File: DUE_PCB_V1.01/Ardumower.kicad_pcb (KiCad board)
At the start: 2 copper layers, 169.3 x 95.5 mm, 86 parts, among them J1 I2C_1, J10 Bumper Left, J11 Bumper Right, J12 P_Left, J13 P_Right, J14 Sonar_R, J15 Sonar_C, J16 Sonar_L, J17 US1, J18 US2, J19 US3, J2 I2C_2, J20 Button, J21 5V IN, J22 Remote, J23 PCB_2, J24 3.3V IN, J25 TX0/RX0, J26 TX1/RX1, J27 TX2/RX2, J28 GPS_TX/GPS_RX, J29 Motor_Right1, J3 I2C_3, J30 Motor_Right2, J31 Motor_Left1, J32 Motor_Left2, J33 Cutter_Motor, J34 ODORight1, J35 ODORight2, J36 ODOLeft1, J37 ODOLeft2, J38 ODOCutter, J4 DS3231 RTC, J5 9V IN, J6 Drop_Left, J7 Drop_Right, J8 Tilt, J9 Rain

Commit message: Start ro add Bernard changes from 1.02
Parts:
- added B1: SPARKFUN_LOGIC_LEVEL_CONVERTER, Boards:SPARKFUN_LOGIC_LEVEL_CONVERTER, F.Cu at (109.3, 83.9)

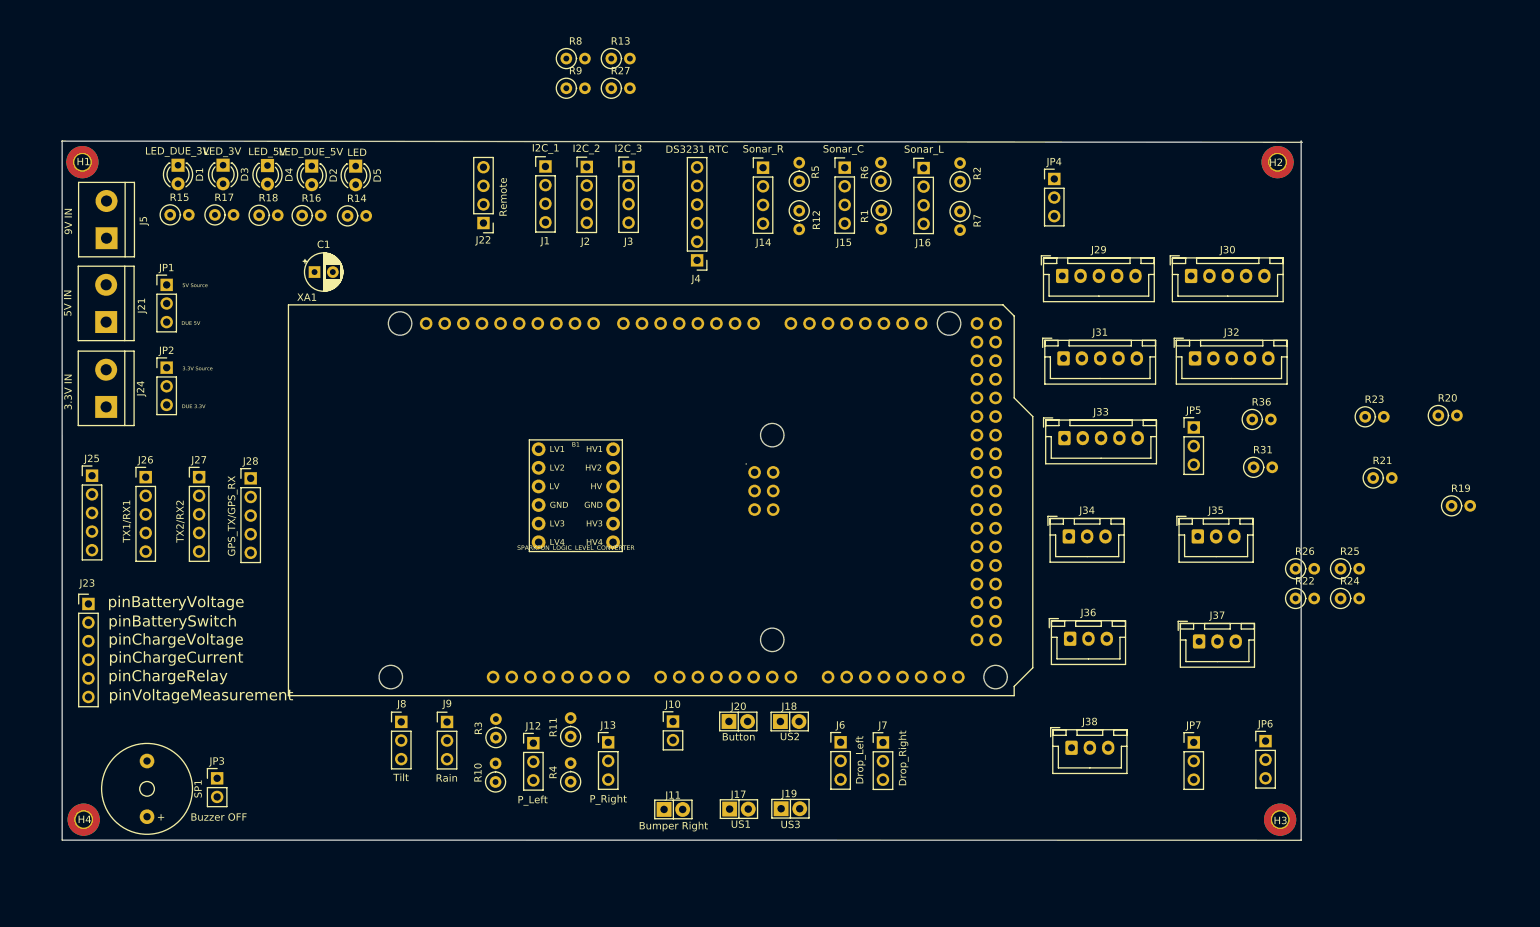
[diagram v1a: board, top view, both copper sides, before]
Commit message: Add Reserve Pin Connectors
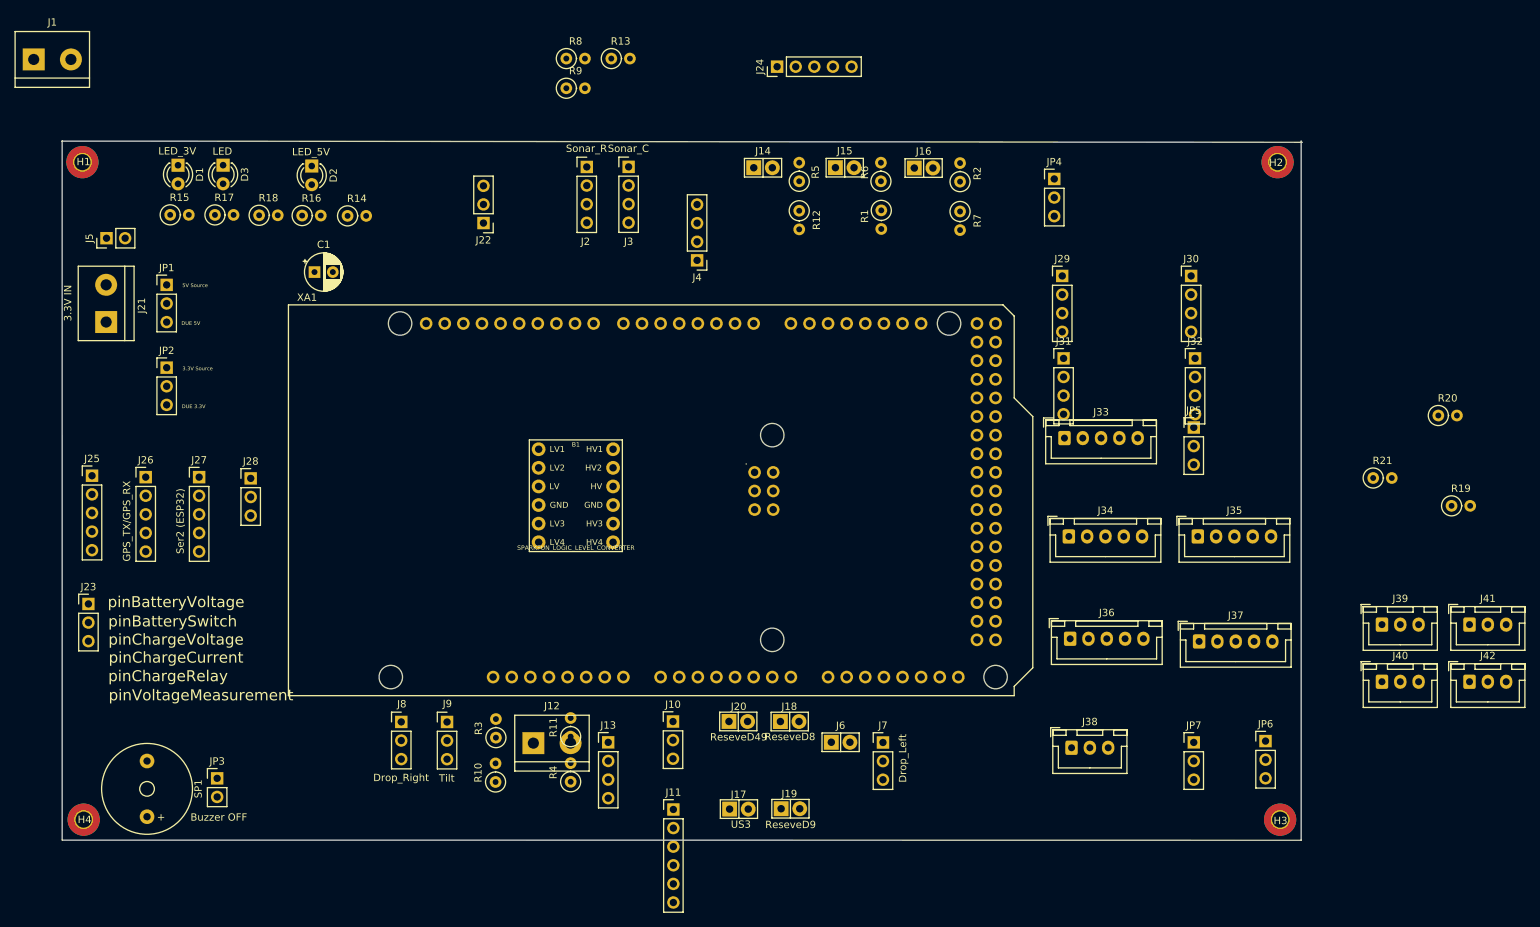
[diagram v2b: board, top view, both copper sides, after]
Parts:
- removed D4: LED_5V, LED_THT:LED_D3.0mm
- removed D5: LED, LED_THT:LED_D3.0mm
- removed R22, R31: 1KO, Resistor_THT:R_Axial_DIN0207_L6.3mm_D2.5mm_P2.54mm_Vertical
- removed R23, R24, R25, R26, R36: 1.5KO, Resistor_THT:R_Axial_DIN0207_L6.3mm_D2.5mm_P2.54mm_Vertical
- removed R27: XXX, Resistor_THT:R_Axial_DIN0207_L6.3mm_D2.5mm_P2.54mm_Vertical
- added J39: ODORight2, Connector_JST:JST_XH_B3B-XH-A_1x03_P2.50mm_Vertical, F.Cu at (219.4, 101.5)
- added J40: ODOLeft1, Connector_JST:JST_XH_B3B-XH-A_1x03_P2.50mm_Vertical, F.Cu at (219.4, 109.3)
- added J41: ODOLeft2, Connector_JST:JST_XH_B3B-XH-A_1x03_P2.50mm_Vertical, F.Cu at (231.3, 101.5)
- added J42: ODOCutter, Connector_JST:JST_XH_B3B-XH-A_1x03_P2.50mm_Vertical, F.Cu at (231.3, 109.3)
- D1: value LED_DUE_3V -> LED_3V
- D2: value LED_DUE_5V -> LED_5V
- D3: value LED_3V -> LED
- J1: value I2C_1 -> 9V IN; footprint Connector_PinHeader_2.54mm:PinHeader_1x04_P2.54mm_Vertical -> TerminalBlock:TerminalBlock_bornier-2_P5.08mm
- J10: value Bumper Left -> Rain; footprint Connector_PinHeader_2.54mm:PinHeader_1x02_P2.54mm_Vertical -> Connector_PinHeader_2.54mm:PinHeader_1x03_P2.54mm_Vertical
- J11: value Bumper Right -> PCB_2; footprint Zimprich:Pin_Header_KK110_1x02_3D -> Connector_PinHeader_2.54mm:PinHeader_1x06_P2.54mm_Vertical
- J12: value P_Left -> 5V IN; footprint Connector_PinHeader_2.54mm:PinHeader_1x03_P2.54mm_Vertical -> TerminalBlock:TerminalBlock_bornier-2_P5.08mm
- J13: value P_Right -> Remote; footprint Connector_PinHeader_2.54mm:PinHeader_1x03_P2.54mm_Vertical -> Connector_PinHeader_2.54mm:PinHeader_1x04_P2.54mm_Vertical
- J14: value Sonar_R -> Button; footprint Connector_PinHeader_2.54mm:PinHeader_1x04_P2.54mm_Vertical -> Zimprich:Pin_Header_KK110_1x02_3D
- J15: value Sonar_C -> US1; footprint Connector_PinHeader_2.54mm:PinHeader_1x04_P2.54mm_Vertical -> Zimprich:Pin_Header_KK110_1x02_3D
- J16: value Sonar_L -> US2; footprint Connector_PinHeader_2.54mm:PinHeader_1x04_P2.54mm_Vertical -> Zimprich:Pin_Header_KK110_1x02_3D
- J17: value US1 -> US3
- J18: value US2 -> ReseveD8
- J19: value US3 -> ReseveD9
- J2: value I2C_2 -> Sonar_R
- J20: value Button -> ReseveD49
- J21: value 5V IN -> 3.3V IN
- J22: value Remote -> P_Left; footprint Connector_PinHeader_2.54mm:PinHeader_1x04_P2.54mm_Vertical -> Connector_PinHeader_2.54mm:PinHeader_1x03_P2.54mm_Vertical
- J23: value PCB_2 -> P_Right; footprint Connector_PinHeader_2.54mm:PinHeader_1x06_P2.54mm_Vertical -> Connector_PinHeader_2.54mm:PinHeader_1x03_P2.54mm_Vertical
- J24: value 3.3V IN -> Ser0; footprint TerminalBlock:TerminalBlock_bornier-2_P5.08mm -> Connector_PinHeader_2.54mm:PinHeader_1x05_P2.54mm_Vertical
- J25: value TX0/RX0 -> Ser1
- J26: value TX1/RX1 -> GPS_TX/GPS_RX
- J27: value TX2/RX2 -> Ser2 (ESP32)
- J28: value GPS_TX/GPS_RX -> Buzzer; footprint Connector_PinHeader_2.54mm:PinHeader_1x05_P2.54mm_Vertical -> Connector_PinHeader_2.54mm:PinHeader_1x03_P2.54mm_Vertical
- J29: value Motor_Right1 -> I2C0_1; footprint Connector_JST:JST_XH_B5B-XH-A_1x05_P2.50mm_Vertical -> Connector_PinHeader_2.54mm:PinHeader_1x04_P2.54mm_Vertical
- J3: value I2C_3 -> Sonar_C
- J30: value Motor_Right2 -> I2C0_2; footprint Connector_JST:JST_XH_B5B-XH-A_1x05_P2.50mm_Vertical -> Connector_PinHeader_2.54mm:PinHeader_1x04_P2.54mm_Vertical
- J31: value Motor_Left1 -> I2C1_1; footprint Connector_JST:JST_XH_B5B-XH-A_1x05_P2.50mm_Vertical -> Connector_PinHeader_2.54mm:PinHeader_1x04_P2.54mm_Vertical
- J32: value Motor_Left2 -> I2C1_2; footprint Connector_JST:JST_XH_B5B-XH-A_1x05_P2.50mm_Vertical -> Connector_PinHeader_2.54mm:PinHeader_1x04_P2.54mm_Vertical
- J33: value Cutter_Motor -> Motor_Right1
- J34: value ODORight1 -> Motor_Right2; footprint Connector_JST:JST_XH_B3B-XH-A_1x03_P2.50mm_Vertical -> Connector_JST:JST_XH_B5B-XH-A_1x05_P2.50mm_Vertical
- J35: value ODORight2 -> Motor_Left1; footprint Connector_JST:JST_XH_B3B-XH-A_1x03_P2.50mm_Vertical -> Connector_JST:JST_XH_B5B-XH-A_1x05_P2.50mm_Vertical
- J36: value ODOLeft1 -> Motor_Left2; footprint Connector_JST:JST_XH_B3B-XH-A_1x03_P2.50mm_Vertical -> Connector_JST:JST_XH_B5B-XH-A_1x05_P2.50mm_Vertical
- J37: value ODOLeft2 -> Cutter_Motor; footprint Connector_JST:JST_XH_B3B-XH-A_1x03_P2.50mm_Vertical -> Connector_JST:JST_XH_B5B-XH-A_1x05_P2.50mm_Vertical
- J38: value ODOCutter -> ODORight1
- J4: value DS3231 RTC -> Sonar_L; footprint Connector_PinHeader_2.54mm:PinHeader_1x06_P2.54mm_Vertical -> Connector_PinHeader_2.54mm:PinHeader_1x04_P2.54mm_Vertical
- J5: value 9V IN -> Bumper Left; footprint TerminalBlock:TerminalBlock_bornier-2_P5.08mm -> Connector_PinHeader_2.54mm:PinHeader_1x02_P2.54mm_Vertical
- J6: value Drop_Left -> Bumper Right; footprint Connector_PinHeader_2.54mm:PinHeader_1x03_P2.54mm_Vertical -> Zimprich:Pin_Header_KK110_1x02_3D
- J7: value Drop_Right -> Drop_Left
- J8: value Tilt -> Drop_Right
- J9: value Rain -> Tilt
- R10, R11: value 1.5KO -> XXX
- R12: value 2KO -> 1KO
- R13: value XXX -> 1KO
- R14, R15: value 100 -> 1KO
- R16: value 220 -> 1KO
- R17: value 100 -> 1.5KO
- R18: value 220 -> 1.5KO
- R19, R20, R21, R3, R4: value 1KO -> 1.5KO
- R5: value 1KO -> XXX
- R6: value 2KO -> XXX
- R7: value 2KO -> 100
- R8: value XXX -> 100
- R9: value XXX -> 220
- moved J24 102.7 mm to (136.8, 25.4)
- moved J1 71.4 mm to (35.3, 24.4)
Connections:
- J1 pad 1: +3V3 -> GND
- J1 pad 2: GND -> +9V
- J10 pad 1: GND -> +3V3
- J10 pad 2: pinBumperLeft -> GND
- J11 pad 1: GND -> pinBatteryVoltage
- J11 pad 2: pinBumperRight -> pinBatterySwitch
- J12 pad 1: +5V -> GND
- J12 pad 2: GND -> Net-(J12-Pad2)
- J13 pad 1: +5V -> pinRemoteSpeed
- J13 pad 2: GND -> pinRemoteSteer
- J13 pad 3: Net-(J13-Pad3) -> pinRemoteMow
- J14 pad 1: +5V -> GND
- J14 pad 2: GND -> pinButton
- J15 pad 1: +5V -> GND
- J15 pad 2: GND -> pinUserSwitch1
- J16 pad 1: +5V -> GND
- J16 pad 2: GND -> pinUserSwitch2
- J17 pad 2: pinUserSwitch1 -> pinUserSwitch3
- J18 pad 2: pinUserSwitch2 -> ReservePinD8
- J19 pad 2: pinUserSwitch3 -> ReservePinD9
- J2 pad 3: SDA0 -> pinSonarRightEcho
- J2 pad 4: SCL0 -> pinSonarRightTrigger
- J20 pad 2: pinButton -> ReservePinD49
- J22 pad 1: pinRemoteSpeed -> +5V
- J22 pad 2: pinRemoteSteer -> GND
- J22 pad 3: pinRemoteMow -> Net-(J22-Pad3)
- J23 pad 1: pinBatteryVoltage -> +5V
- J23 pad 2: pinBatterySwitch -> GND
- J23 pad 3: pinChargeVoltage -> Net-(J23-Pad3)
- J24 pad 1: GND -> +3V3
- J24 pad 2: Net-(J24-Pad2) -> GND
- J25 pad 3: RX0 -> RX1
- J25 pad 4: TX0 -> TX1
- J26 pad 3: RX1 -> (no net)
- J26 pad 4: TX1 -> TX3
- J28 pad 3: GPS_RX -> pinBuzzer
- J29 pad 1: pinMotorRightPWM -> +3V3
- J29 pad 2: pinMotorRightDir -> GND
- J29 pad 3: pinMotorEnable -> SDA0
- J29 pad 4: Net-(J29-Pad4) -> SCL0
- J3 pad 3: SDA1 -> pinSonarCenterEcho
- J3 pad 4: SCL1 -> pinSonarCenterTrigger
- J30 pad 1: pinMotorRight2PWM -> +3V3
- J30 pad 2: pinMotorRightDir -> GND
- J30 pad 3: pinMotorEnable -> SDA0
- J30 pad 4: Net-(J29-Pad4) -> SCL0
- J31 pad 1: pinMotorLeftPWM -> +3V3
- J31 pad 2: pinMotorLeftDir -> GND
- J31 pad 3: pinMotorEnable -> SDA1
- J31 pad 4: Net-(J29-Pad4) -> SCL1
- J32 pad 1: pinMotorLeft2PWM -> +3V3
- J32 pad 2: pinMotorLeftDir -> GND
- J32 pad 3: pinMotorEnable -> SDA1
- J32 pad 4: Net-(J29-Pad4) -> SCL1
- J33 pad 1: pinMotorMowPWM -> pinMotorRightPWM
- J33 pad 2: pinMotorMowDir -> pinMotorRightDir
- J33 pad 3: pinMotorMowEnable -> pinMotorEnable
- J34 pad 1: Net-(J34-Pad1) -> pinMotorRight2PWM
- J34 pad 2: Net-(J34-Pad2) -> pinMotorRight2Dir
- J34 pad 3: GND -> pinMotorEnable
- J35 pad 1: Net-(J35-Pad1) -> pinMotorLeftPWM
- J35 pad 2: Net-(J34-Pad2) -> pinMotorLeftDir
- J35 pad 3: GND -> pinMotorEnable
- J36 pad 1: Net-(J36-Pad1) -> pinMotorLeft2PWM
- J36 pad 2: Net-(J34-Pad2) -> pinMotorLeft2Dir
- J36 pad 3: GND -> pinMotorEnable
- J37 pad 1: Net-(J37-Pad1) -> pinMotorMowPWM
- J37 pad 2: Net-(J34-Pad2) -> pinMotorMowDir
- J37 pad 3: GND -> pinMotorMowEnable
- J4 pad 1: (no net) -> +3V3
- J4 pad 2: (no net) -> GND
- J4 pad 3: SCL1 -> pinSonarLeftEcho
- J4 pad 4: SDA1 -> pinSonarLeftTrigger
- J5 pad 2: +9V -> pinBumperLeft
- J6 pad 1: +3V3 -> GND
- J6 pad 2: GND -> pinBumperRight
- J7 pad 3: pinDropRight -> pinDropLeft
- J8 pad 3: pinTilt -> pinDropRight
- J9 pad 3: pinRain -> pinTilt
- JP1 pad 1: Net-(J21-Pad2) -> Net-(J12-Pad2)
- JP2 pad 1: Net-(J24-Pad2) -> Net-(J21-Pad2)
- JP4 pad 2: Net-(J29-Pad4) -> Net-(J33-Pad4)
- JP5 pad 2: Net-(J33-Pad4) -> Net-(J37-Pad4)
- JP6 pad 2: Net-(J34-Pad2) -> Net-(J38-Pad2)
- JP7 pad 2: Net-(J38-Pad2) -> Net-(J42-Pad2)
- R1 pad 1: Net-(J15-Pad3) -> Net-(J22-Pad3)
- R1 pad 2: pinSonarCenterEcho -> pinPerimeterLeft
- R10 pad 1: Net-(J12-Pad3) -> SDA0
- R10 pad 2: GND -> +3V3
- R11 pad 1: Net-(J13-Pad3) -> SDA1
- R11 pad 2: GND -> +3V3
- R12 pad 1: Net-(J14-Pad3) -> pinOdometryRight
- R12 pad 2: GND -> Net-(J38-Pad1)
- R13 pad 1: SDA0 -> pinOdometryRight2
- R13 pad 2: +3V3 -> Net-(J39-Pad1)
- R14 pad 1: pinLED -> pinOdometryLeft
- R14 pad 2: Net-(D5-Pad2) -> Net-(J40-Pad1)
- R15 pad 1: Net-(D1-Pad2) -> pinOdometryLeft2
- R15 pad 2: DUE_3.3V -> Net-(J41-Pad1)
- R16 pad 1: Net-(D2-Pad2) -> pinMotorMowRpm
- R16 pad 2: DUE_5V -> Net-(J42-Pad1)
- R17 pad 1: Net-(D3-Pad2) -> Net-(J38-Pad1)
- R17 pad 2: +3V3 -> GND
- R18 pad 1: Net-(D4-Pad2) -> Net-(J39-Pad1)
- R18 pad 2: +5V -> GND
- R19 pad 1: pinOdometryRight2 -> Net-(J40-Pad1)
- R19 pad 2: Net-(J35-Pad1) -> GND
- R2 pad 1: Net-(J16-Pad3) -> Net-(J23-Pad3)
- R2 pad 2: pinSonarLeftEcho -> pinPerimeterRight
- R20 pad 1: pinOdometryLeft -> Net-(J41-Pad1)
- R20 pad 2: Net-(J36-Pad1) -> GND
- R21 pad 1: pinOdometryLeft2 -> Net-(J42-Pad1)
- R21 pad 2: Net-(J37-Pad1) -> GND
- R3 pad 1: Net-(J12-Pad3) -> Net-(J22-Pad3)
- R3 pad 2: pinPerimeterLeft -> GND
- R4 pad 1: Net-(J13-Pad3) -> Net-(J23-Pad3)
- R4 pad 2: pinPerimeterRight -> GND
- R5 pad 1: Net-(J14-Pad3) -> SCL0
- R5 pad 2: pinSonarRightEcho -> +3V3
- R6 pad 1: Net-(J15-Pad3) -> SCL1
- R6 pad 2: GND -> +3V3
- R7 pad 1: Net-(J16-Pad3) -> pinLED
- R7 pad 2: GND -> Net-(D3-Pad2)
- R8 pad 1: SCL0 -> Net-(D1-Pad2)
- R9 pad 1: SCL1 -> Net-(D2-Pad2)
- R9 pad 2: +3V3 -> +5V
- XA1 pad D14: GPS_RX -> RX2
- XA1 pad D15: GPS_TX -> TX3
- XA1 pad D40: (no net) -> pinMotorLeft2Dir
- XA1 pad D41: (no net) -> pinMotorRight2Dir
- XA1 pad D49: (no net) -> ReservePinD49
- XA1 pad D8: (no net) -> ReservePinD8
- XA1 pad D9: (no net) -> ReservePinD9

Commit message: Change Pin Header to JST
Change Pin Header to JST and sort them on the PCB
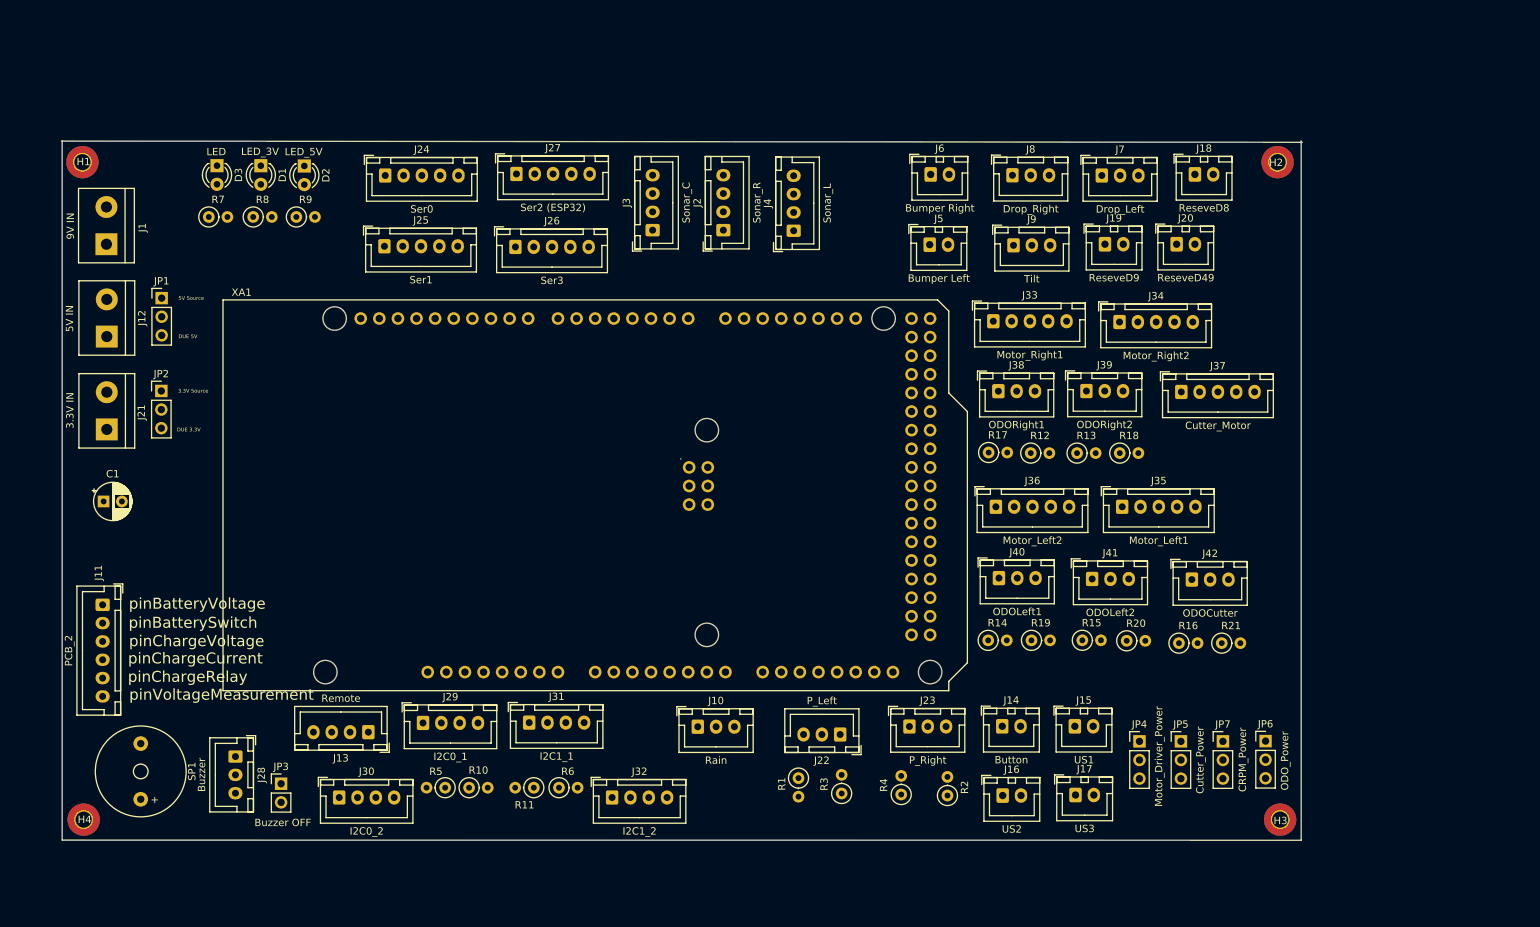
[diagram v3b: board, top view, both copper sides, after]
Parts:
- removed B1: SPARKFUN_LOGIC_LEVEL_CONVERTER, Boards:SPARKFUN_LOGIC_LEVEL_CONVERTER
- J10, J22, J23, J28, J7, J8, J9: footprint Connector_PinHeader_2.54mm:PinHeader_1x03_P2.54mm_Vertical -> Connector_JST:JST_XH_B3B-XH-A_1x03_P2.50mm_Vertical
- J11: footprint Connector_PinHeader_2.54mm:PinHeader_1x06_P2.54mm_Vertical -> Connector_JST:JST_XH_B6B-XH-A_1x06_P2.50mm_Vertical
- J13, J2, J29, J3, J30, J31, J32, J4: footprint Connector_PinHeader_2.54mm:PinHeader_1x04_P2.54mm_Vertical -> Connector_JST:JST_XH_B4B-XH-A_1x04_P2.50mm_Vertical
- J14, J15, J16, J17, J18, J19, J20, J6: footprint Zimprich:Pin_Header_KK110_1x02_3D -> Connector_JST:JST_XH_B2B-XH-A_1x02_P2.50mm_Vertical
- J24, J25, J27: footprint Connector_PinHeader_2.54mm:PinHeader_1x05_P2.54mm_Vertical -> Connector_JST:JST_XH_B5B-XH-A_1x05_P2.50mm_Vertical
- J26: value GPS_TX/GPS_RX -> Ser3; footprint Connector_PinHeader_2.54mm:PinHeader_1x05_P2.54mm_Vertical -> Connector_JST:JST_XH_B5B-XH-A_1x05_P2.50mm_Vertical
- J5: footprint Connector_PinHeader_2.54mm:PinHeader_1x02_P2.54mm_Vertical -> Connector_JST:JST_XH_B2B-XH-A_1x02_P2.50mm_Vertical
- moved R15 137.4 mm to (178.5, 103.7)
- moved J30 136.3 mm to (77.0, 125.1)
- moved R16 133.2 mm to (191.7, 104.0)
- moved R18 121.9 mm to (183.6, 78.1)
- moved J23 113.3 mm to (154.9, 115.4)
- moved J5 112.4 mm to (157.6, 49.6), turned to 0 degrees
- moved J8 111.9 mm to (168.9, 40.2)
- moved R17 110.5 mm to (165.7, 78.0)
- moved J29 106.5 mm to (88.5, 114.9)
- moved R14 104.9 mm to (165.6, 103.7)
- moved R7 102.5 mm to (59.2, 45.9), turned to 0 degrees
- moved J9 101.1 mm to (169.1, 49.7)
- moved J32 99.6 mm to (114.3, 125.1)
- moved R5 95.8 mm to (91.5, 123.8), turned to 180 degrees
- moved R6 93.7 mm to (107.0, 123.8), turned to 0 degrees
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
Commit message: Add PCB Pin Description
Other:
- net class 24v added: clearance 0.254, trace_width 0.5, via_dia 0.889, via_drill 0.635
- net class 9v added: clearance 0.254, trace_width 0.254, via_dia 0.889, via_drill 0.635
- net class Default: clearance 0.2 -> 0.254; trace_width 0.25 -> 0.254; via_dia 0.8 -> 0.889; via_drill 0.4 -> 0.635
- rule trace_clearance: 0.2 -> 0.254
- rule trace_min: 0.2 -> 0.254
- rule via_min_drill: 0.3 -> 0.508
- rule via_min_size: 0.4 -> 0.889
